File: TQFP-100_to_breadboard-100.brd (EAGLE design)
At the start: 147.4 x 22.9 mm, 5 parts, among them J1 CONNECTOR_25, J2 CONNECTOR_25_NO_SQUARE, J3 CONNECTOR_25_NO_SQUARE, J4 CONNECTOR_25_NO_SQUARE, U1 IC-GENERIC-100-TQFP

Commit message: continuing work on the TQFP-100 routing.
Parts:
- moved J3 74.2 mm to (72.4, 7.62)
- moved J1 74.2 mm to (-72.4, -7.62)
- moved J2 74.2 mm to (11.4, -7.62)
- moved J4 74.2 mm to (-11.4, 7.62)
- moved U1 74.2 mm to (0.00, 0.00)
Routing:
- net N$2: track 68.5 -> 0.00 mm, vias 1 -> 0
- net N$4: track 64.4 -> 0.00 mm, vias 1 -> 0
- net N$98: track 0.00 -> 63.7 mm
- net N$5: track 59.2 -> 0.00 mm
- net N$96: track 0.00 -> 59.1 mm
- net N$7: track 54.6 -> 0.00 mm
- net N$94: track 0.00 -> 54.5 mm
- net N$10: track 51.9 -> 0.00 mm, vias 1 -> 0
- net N$9: track 50.0 -> 0.00 mm
- net N$92: track 0.00 -> 49.9 mm
- net N$12: track 47.7 -> 0.00 mm, vias 1 -> 0
- net N$11: track 45.4 -> 0.00 mm
- net N$90: track 0.00 -> 45.3 mm
- net N$14: track 43.4 -> 0.00 mm, vias 1 -> 0
- net N$13: track 40.9 -> 0.00 mm
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
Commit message: continuing routing traces.
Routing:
- net N$52: track 0.00 -> 68.0 mm, vias 0 -> 1
- net N$49: track 0.00 -> 67.9 mm, vias 0 -> 1
- net N$51: track 0.00 -> 67.8 mm
- net N$50: track 0.00 -> 67.8 mm
- net N$99: track 0.00 -> 67.6 mm, vias 0 -> 1
- net N$2: track 0.00 -> 67.5 mm, vias 0 -> 1
- net N$53: track 0.00 -> 63.9 mm
- net N$48: track 0.00 -> 63.7 mm
- net N$54: track 0.00 -> 63.5 mm, vias 0 -> 1
- net N$47: track 0.00 -> 63.2 mm, vias 0 -> 1
- net N$4: track 0.00 -> 63.0 mm, vias 0 -> 1
- net N$97: track 0.00 -> 62.2 mm, vias 0 -> 1
- net N$5: track 0.00 -> 59.1 mm
- net N$55: track 0.00 -> 59.1 mm
- net N$46: track 0.00 -> 59.1 mm
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
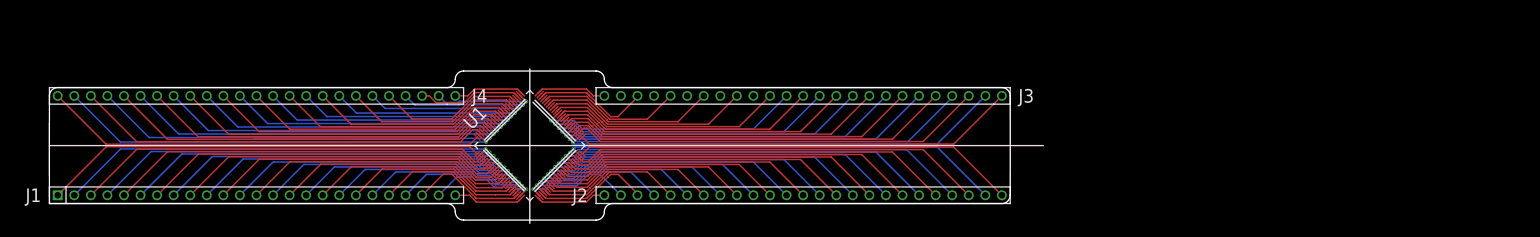
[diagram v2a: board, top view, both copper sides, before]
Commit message: finished TQFP-100
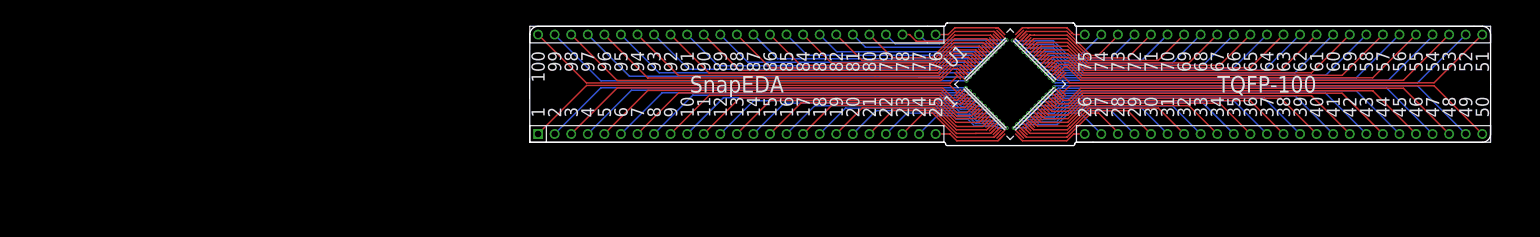
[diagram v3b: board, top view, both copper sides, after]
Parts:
- U1: value IC-GENERIC-100-TQFP -> (none)
- moved J3 74.3 mm to (146.1, 17.0)
- moved J1 74.3 mm to (1.27, 1.78)
- moved J2 74.3 mm to (85.1, 1.78)
- moved J4 74.3 mm to (62.2, 17.0)
- moved U1 74.3 mm to (73.7, 9.40)
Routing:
- net N$66: track 0.00 -> 35.8 mm, vias 0 -> 1
- net N$68: track 0.00 -> 31.4 mm, vias 0 -> 1
- net N$70: track 0.00 -> 26.5 mm, vias 0 -> 1
- net N$72: track 0.00 -> 22.0 mm, vias 0 -> 1
- net N$74: track 0.00 -> 17.5 mm, vias 0 -> 1
- net N$97: track 62.2 -> 63.1 mm
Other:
- board size 147.4 x 22.9 mm -> 147.4 x 18.8 mm
- board text added: "1"
- board text added: "10"
- board text added: "100"
- board text added: "11"
- board text added: "12"
- board text added: "13"
- board text added: "14"
- board text added: "15"
- board text added: "16"
- board text added: "17"
- board text added: "18"
- board text added: "19"
- board text added: "2"
- board text added: "20"
- board text added: "21"
- board text added: "22"
- board text added: "23"
- board text added: "24"
- board text added: "25"
- board text added: "26"
- board text added: "27"
- board text added: "28"
- board text added: "29"
- board text added: "3"
- board text added: "30"
- board text added: "31"
- board text added: "32"
- board text added: "33"
- board text added: "34"
- board text added: "35"
- board text added: "36"
- board text added: "37"
- board text added: "38"
- board text added: "39"
- board text added: "4"
- board text added: "40"
- board text added: "41"
- board text added: "42"
- board text added: "43"
- board text added: "44"
- board text added: "45"
- board text added: "46"
- board text added: "47"
- board text added: "48"
- board text added: "49"
- board text added: "5"
- board text added: "50"
- board text added: "51"
- board text added: "52"
- board text added: "53"
- board text added: "54"
- board text added: "55"
- board text added: "56"
- board text added: "57"
- board text added: "58"
- board text added: "59"
- board text added: "6"
- board text added: "60"
- board text added: "61"
- board text added: "62"
- board text added: "63"
- board text added: "64"
- board text added: "65"
- board text added: "66"
- board text added: "67"
- board text added: "68"
- board text added: "69"
- board text added: "7"
- board text added: "70"
- board text added: "71"
- board text added: "72"
- board text added: "73"
- board text added: "74"
- board text added: "75"
- board text added: "76"
- board text added: "77"
- board text added: "78"
- board text added: "79"
- board text added: "8"
- board text added: "80"
- board text added: "81"
- board text added: "82"
- board text added: "83"
- board text added: "84"
- board text added: "85"
- board text added: "86"
- board text added: "87"
- board text added: "88"
- board text added: "89"
- board text added: "9"
- board text added: "90"
- board text added: "91"
- board text added: "92"
- board text added: "93"
- board text added: "94"
- board text added: "95"
- board text added: "96"
- board text added: "97"
- board text added: "98"
- board text added: "99"
- board text added: "TQFP-100"
- board text removed: "QFN-16"
